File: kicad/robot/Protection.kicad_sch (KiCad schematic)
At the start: 44 parts, among them IC1 TPS22998RYZR, Q1 Q_NMOS_GDS, Q2 EFC8811R-TF, SW1 SW_SPST, U12 BQ27742YZFR-G1

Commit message: BOM exclusions for net ties and n/a part test points
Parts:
- TP28, TP29: now left out of the parts list
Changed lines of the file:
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@@
   )
   (symbol (lib_id "robot:TestPoint") (at 394.97 80.01 0) (unit 1)
-    (in_bom yes) (on_board yes) (dnp no) (fields_autoplaced)
+    (in_bom no) (on_board yes) (dnp no) (fields_autoplaced)
     (property "Reference" "TP29" (at 397.51 76.708 0)
       (effects (font (size 1.27 1.27)) (justify left))
@@
   )
   (symbol (lib_id "robot:TestPoint") (at 43.18 133.35 90) (unit 1)
-    (in_bom yes) (on_board yes) (dnp no) (fields_autoplaced)
+    (in_bom no) (on_board yes) (dnp no) (fields_autoplaced)
     (property "Reference" "TP28" (at 39.878 130.81 90)
       (effects (font (size 1.27 1.27)))

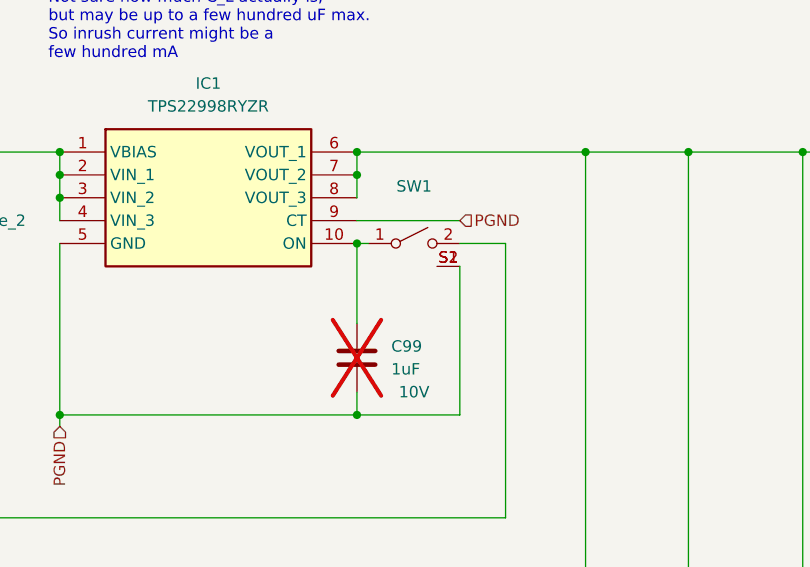
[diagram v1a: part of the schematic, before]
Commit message: Switch wasn't added for some reason
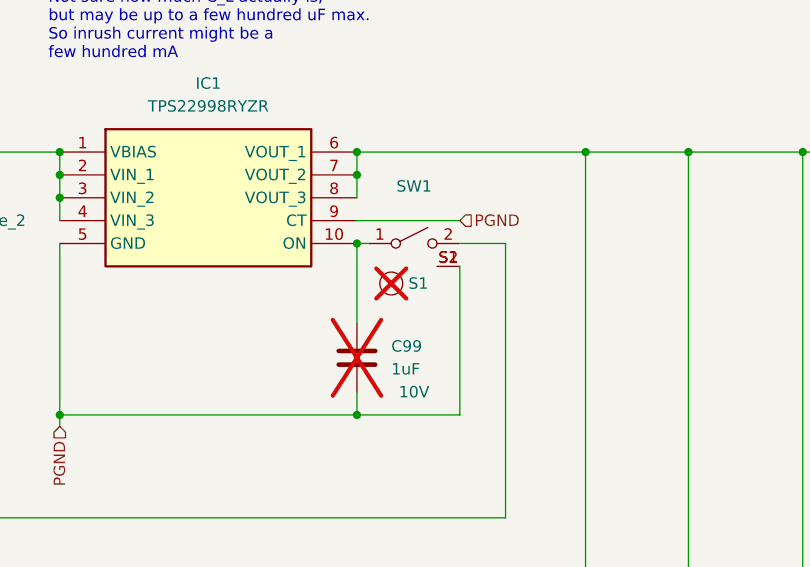
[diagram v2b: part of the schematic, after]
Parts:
- added S1: ~, symbol robot:SW-R3-1A-A-1-2
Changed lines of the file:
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@@
+    )
+  )
+  (symbol (lib_id "robot:SW-R3-1A-A-1-2") (at 319.405 95.885 0) (unit 1)
+    (in_bom yes) (on_board no) (dnp yes) (fields_autoplaced)
+    (property "Reference" "S1" (at 321.31 95.885 0)
+      (effects (font (size 1.27 1.27)) (justify left))
+    )
+    (property "Value" "~" (at 319.405 95.885 0)
+      (effects (font (size 1.27 1.27)) hide)
+    )
+    (property "Footprint" "" (at 319.405 95.885 0)
+      (effects (font (size 1.27 1.27)) hide)
+    )
+    (property "Datasheet" "https://app.adam-tech.com/products/download/data_sheet/203477/sw-r3-1a-a-xx-2-data-sheet.pdf" (at 319.405 95.885 0)
+      (effects (font (size 1.27 1.27)) hide)
+    )
+    (property "Manufacturer" "Adam Tech" (at 319.405 95.885 0)
+      (effects (font (size 1.27 1.27)) hide)
+    )
+    (property "Part Number" "SW-R3-1A-A-1-2" (at 319.405 95.885 0)
+      (effects (font (size 1.27 1.27)) hide)
+    )
+    (instances
+      (project "robot"
+        (path "/0c7b298e-2d07-4b1f-b033-e95f02d45089/aaf20b87-68dc-43c9-a7d3-4ceda8b87424"
+          (reference "S1") (unit 1)
+        )
+      )
     )
   )

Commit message: Updating part number for 0805 100uF caps
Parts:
- C106, C107, C108, C96, C98: Part Number GRM31CD80J107MEA8K -> GRM21BR60E107ME15K
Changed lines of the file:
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@@
       (effects (font (size 1.27 1.27)) hide)
     )
-    (property "Part Number" "GRM31CD80J107MEA8K" (at 365.125 138.43 0)
+    (property "Part Number" "GRM21BR60E107ME15K" (at 365.125 138.43 0)
       (effects (font (size 1.27 1.27)) hide)
     )
@@
       (effects (font (size 1.27 1.27)) hide)
     )
-    (property "Part Number" "GRM31CD80J107MEA8K" (at 264.16 138.43 0)
+    (property "Part Number" "GRM21BR60E107ME15K" (at 264.16 138.43 0)
       (effects (font (size 1.27 1.27)) hide)
     )
@@
       (effects (font (size 1.27 1.27)) hide)
     )
-    (property "Part Number" "GRM31CD80J107MEA8K" (at 352.425 138.43 0)
+    (property "Part Number" "GRM21BR60E107ME15K" (at 352.425 138.43 0)
       (effects (font (size 1.27 1.27)) hide)
     )
@@
       (effects (font (size 1.27 1.27)) hide)
     )
-    (property "Part Number" "GRM31CD80J107MEA8K" (at 378.46 138.43 0)
+    (property "Part Number" "GRM21BR60E107ME15K" (at 378.46 138.43 0)
       (effects (font (size 1.27 1.27)) hide)
     )
@@
       (effects (font (size 1.27 1.27)) hide)
     )
-    (property "Part Number" "GRM31CD80J107MEA8K" (at 340.995 138.43 0)
-      (effects (font (size 1.27 1.27)) hide)
-    )
+    (property "Part Number" "GRM21BR60E107ME15K" (at 340.995 138.43 0)
+      (effects (font (size 1.27 1.27)) hide)
+    )

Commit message: All BOM and footprints other than 100uF selected
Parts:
- C106, C107, C108, C96, C98: Part Number GRM21BR60E107ME15K -> (none)
- R43, R45: Manufacturer Panasonic Electronic Components -> Panasonic; Part Number ERJ-PA3F2000V -> ERJ-PA3J201V
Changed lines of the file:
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@@
       (effects (font (size 1.27 1.27)) hide)
     )
-    (property "Part Number" "GRM21BR60E107ME15K" (at 365.125 138.43 0)
+    (property "Part Number" "" (at 365.125 138.43 0)
       (effects (font (size 1.27 1.27)) hide)
     )
@@
       (effects (font (size 1.27 1.27)) hide)
     )
-    (property "Part Number" "GRM21BR60E107ME15K" (at 264.16 138.43 0)
+    (property "Part Number" "" (at 264.16 138.43 0)
       (effects (font (size 1.27 1.27)) hide)
     )
@@
       (effects (font (size 1.27 1.27)) hide)
     )
-    (property "Part Number" "GRM21BR60E107ME15K" (at 352.425 138.43 0)
+    (property "Part Number" "" (at 352.425 138.43 0)
       (effects (font (size 1.27 1.27)) hide)
     )
@@
       (effects (font (size 1.27 1.27)) hide)
     )
-    (property "Manufacturer" "Panasonic Electronic Components" (at 150.495 98.425 0)
-      (effects (font (size 1.27 1.27)) hide)
-    )
-    (property "Part Number" "ERJ-PA3F2000V" (at 150.495 98.425 0)
+    (property "Manufacturer" "Panasonic" (at 150.495 98.425 0)
+      (effects (font (size 1.27 1.27)) hide)
+    )
+    (property "Part Number" "ERJ-PA3J201V" (at 150.495 98.425 0)
       (effects (font (size 1.27 1.27)) hide)
     )
@@
       (effects (font (size 1.27 1.27)) hide)
     )
-    (property "Part Number" "GRM21BR60E107ME15K" (at 378.46 138.43 0)
+    (property "Part Number" "" (at 378.46 138.43 0)
       (effects (font (size 1.27 1.27)) hide)
     )
@@
       (effects (font (size 1.27 1.27)) hide)
     )
-    (property "Part Number" "GRM21BR60E107ME15K" (at 340.995 138.43 0)
+    (property "Part Number" "" (at 340.995 138.43 0)
       (effects (font (size 1.27 1.27)) hide)
     )
@@
       (effects (font (size 1.27 1.27)) hide)
     )
-    (property "Manufacturer" "Panasonic Electronic Components" (at 170.815 98.425 0)
-      (effects (font (size 1.27 1.27)) hide)
-    )
-    (property "Part Number" "ERJ-PA3F2000V" (at 170.815 98.425 0)
-      (effects (font (size 1.27 1.27)) hide)
-    )
+    (property "Manufacturer" "Panasonic" (at 170.815 98.425 0)
+      (effects (font (size 1.27 1.27)) hide)
+    )
+    (property "Part Number" "ERJ-PA3J201V" (at 170.815 98.425 0)
+      (effects (font (size 1.27 1.27)) hide)
+    )

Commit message: Updated 100uF caps to 1206 footprint to allow for 6.3V ratings
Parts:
- C106, C107, C108, C96, C98: footprint robot:C_0805_2012Metric -> robot:C_1206_3216Metric; Part Number (none) -> GRM31CD80J107MEA8K
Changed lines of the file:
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@@
       (effects (font (size 1.27 1.27)) (justify left))
     )
-    (property "Footprint" "robot:C_0805_2012Metric" (at 366.0902 142.24 0)
+    (property "Footprint" "robot:C_1206_3216Metric" (at 366.0902 142.24 0)
       (effects (font (size 1.27 1.27)) hide)
     )
@@
       (effects (font (size 1.27 1.27)) hide)
     )
-    (property "Part Number" "" (at 365.125 138.43 0)
+    (property "Part Number" "GRM31CD80J107MEA8K" (at 365.125 138.43 0)
       (effects (font (size 1.27 1.27)) hide)
     )
@@
       (effects (font (size 1.27 1.27)) (justify left))
     )
-    (property "Footprint" "robot:C_0805_2012Metric" (at 265.1252 142.24 0)
+    (property "Footprint" "robot:C_1206_3216Metric" (at 265.1252 142.24 0)
       (effects (font (size 1.27 1.27)) hide)
     )
@@
       (effects (font (size 1.27 1.27)) hide)
     )
-    (property "Part Number" "" (at 264.16 138.43 0)
+    (property "Part Number" "GRM31CD80J107MEA8K" (at 264.16 138.43 0)
       (effects (font (size 1.27 1.27)) hide)
     )
@@
       (effects (font (size 1.27 1.27)) (justify left))
     )
-    (property "Footprint" "robot:C_0805_2012Metric" (at 353.3902 142.24 0)
+    (property "Footprint" "robot:C_1206_3216Metric" (at 353.3902 142.24 0)
       (effects (font (size 1.27 1.27)) hide)
     )
@@
       (effects (font (size 1.27 1.27)) hide)
     )
-    (property "Part Number" "" (at 352.425 138.43 0)
+    (property "Part Number" "GRM31CD80J107MEA8K" (at 352.425 138.43 0)
       (effects (font (size 1.27 1.27)) hide)
     )
@@
       (effects (font (size 1.27 1.27)) (justify left))
     )
-    (property "Footprint" "robot:C_0805_2012Metric" (at 379.4252 142.24 0)
+    (property "Footprint" "robot:C_1206_3216Metric" (at 379.4252 142.24 0)
       (effects (font (size 1.27 1.27)) hide)
     )
@@
       (effects (font (size 1.27 1.27)) hide)
     )
-    (property "Part Number" "" (at 378.46 138.43 0)
+    (property "Part Number" "GRM31CD80J107MEA8K" (at 378.46 138.43 0)
       (effects (font (size 1.27 1.27)) hide)
     )
@@
       (effects (font (size 1.27 1.27)) (justify left))
     )
-    (property "Footprint" "robot:C_0805_2012Metric" (at 341.9602 142.24 0)
+    (property "Footprint" "robot:C_1206_3216Metric" (at 341.9602 142.24 0)
       (effects (font (size 1.27 1.27)) hide)
     )
@@
       (effects (font (size 1.27 1.27)) hide)
     )
-    (property "Part Number" "" (at 340.995 138.43 0)
-      (effects (font (size 1.27 1.27)) hide)
-    )
+    (property "Part Number" "GRM31CD80J107MEA8K" (at 340.995 138.43 0)
+      (effects (font (size 1.27 1.27)) hide)
+    )

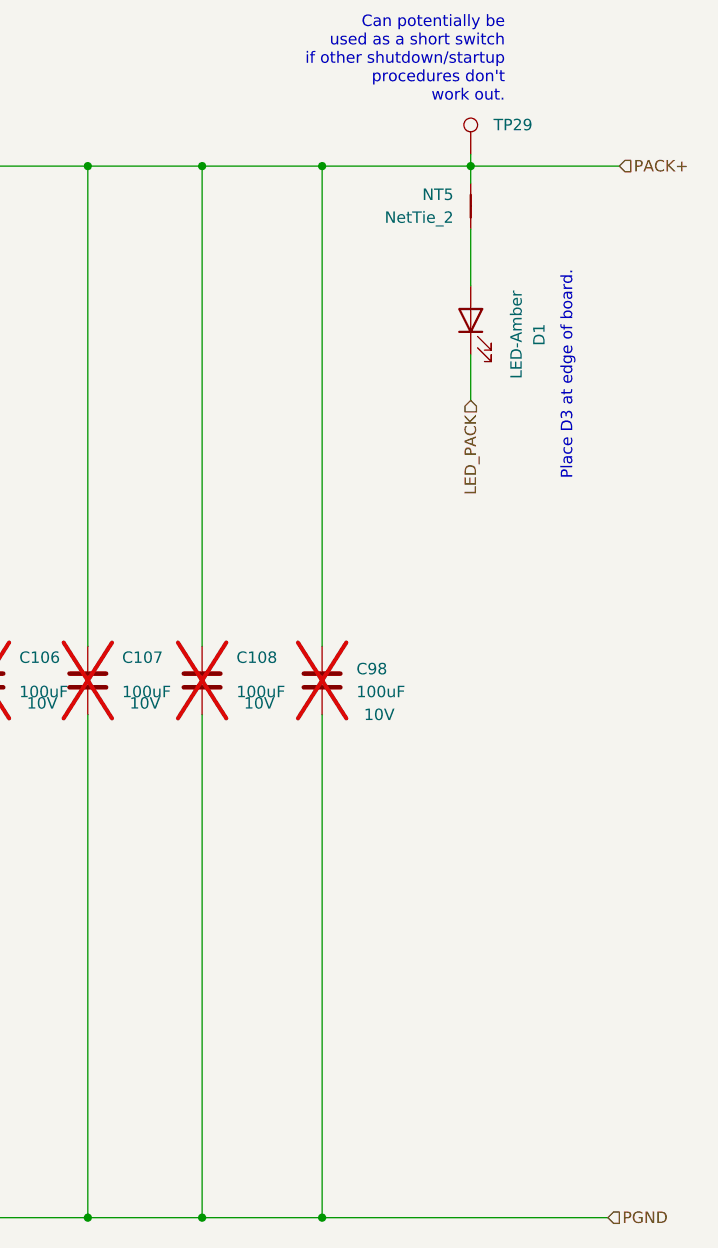
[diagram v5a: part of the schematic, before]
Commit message: Adding wireless charger circuit
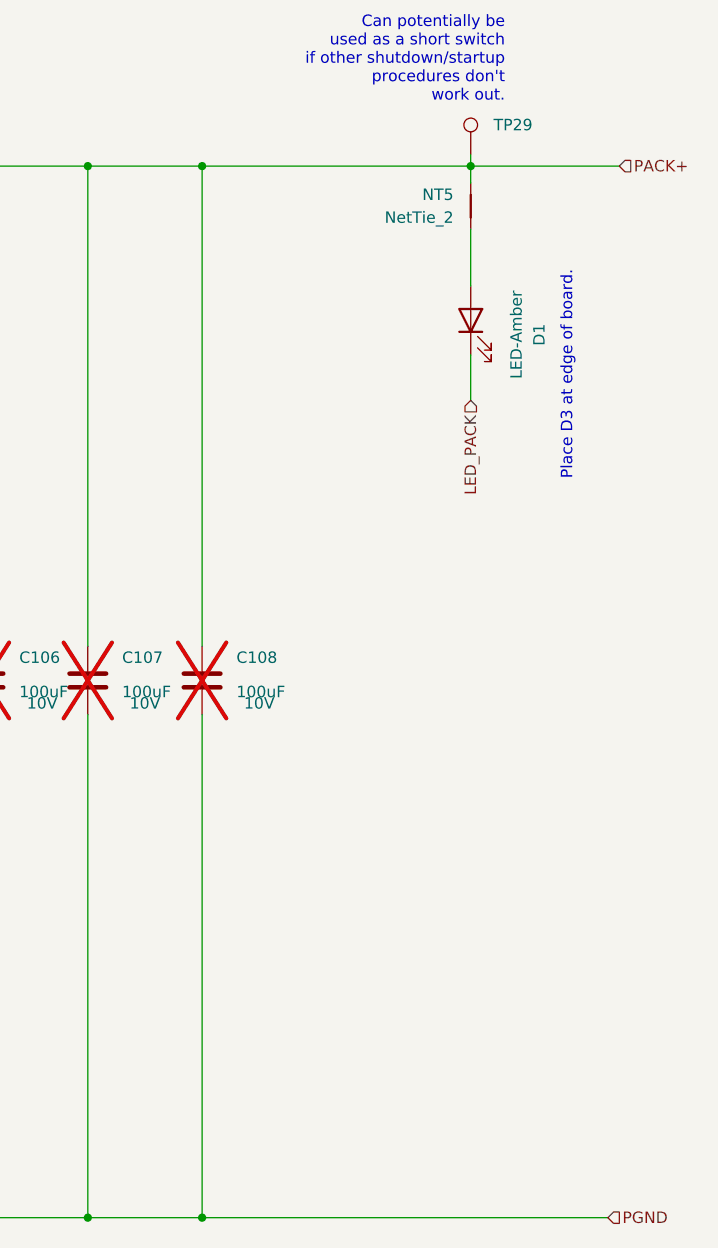
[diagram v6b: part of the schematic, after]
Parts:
- removed C98: 100uF, robot:C_1206_3216Metric, symbol robot:C
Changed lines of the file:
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@@
   (junction (at 282.575 81.28) (diameter 0) (color 0 0 0 0)
   )
-  (junction (at 378.46 81.28) (diameter 0) (color 0 0 0 0)
-  )
   (junction (at 227.965 135.89) (diameter 0) (color 0 0 0 0)
   )
@@
   )
   (junction (at 352.425 81.28) (diameter 0) (color 0 0 0 0)
-  )
-  (junction (at 378.46 198.12) (diameter 0) (color 0 0 0 0)
   )
   (junction (at 170.815 81.28) (diameter 0) (color 0 0 0 0)
@@
     (stroke (width 0) (type default))
   )
-  (wire (pts (xy 378.46 198.12) (xy 410.21 198.12))
+  (wire (pts (xy 365.125 198.12) (xy 410.21 198.12))
     (stroke (width 0) (type default))
   )
@@
     (stroke (width 0) (type default))
   )
-  (wire (pts (xy 378.46 142.24) (xy 378.46 198.12))
-    (stroke (width 0) (type default))
-  )
   (wire (pts (xy 43.18 81.28) (xy 150.495 81.28))
     (stroke (width 0) (type default))
@@
     (stroke (width 0) (type default))
   )
-  (wire (pts (xy 378.46 81.28) (xy 394.97 81.28))
+  (wire (pts (xy 365.125 81.28) (xy 394.97 81.28))
     (stroke (width 0) (type default))
   )
@@
     (stroke (width 0) (type default))
   )
-  (wire (pts (xy 365.125 81.28) (xy 378.46 81.28))
-    (stroke (width 0) (type default))
-  )
   (wire (pts (xy 203.2 101.6) (xy 203.2 109.22))
     (stroke (width 0) (type default))
@@
     (stroke (width 0) (type default))
   )
-  (wire (pts (xy 378.46 81.28) (xy 378.46 134.62))
-    (stroke (width 0) (type default))
-  )
   (wire (pts (xy 140.97 156.21) (xy 158.75 156.21))
     (stroke (width 0) (type default))
@@
   )
   (wire (pts (xy 315.595 91.44) (xy 316.865 91.44))
-    (stroke (width 0) (type default))
-  )
-  (wire (pts (xy 365.125 198.12) (xy 378.46 198.12))
     (stroke (width 0) (type default))
   )
@@
         )
       )
-    )
-  )
-  (symbol (lib_id "robot:C") (at 378.46 138.43 0) (unit 1)
-    (in_bom yes) (on_board yes) (dnp yes)
-    (property "Reference" "C98" (at 382.27 137.1599 0)
-      (effects (font (size 1.27 1.27)) (justify left))
-    )
-    (property "Value" "100uF" (at 382.27 139.6999 0)
-      (effects (font (size 1.27 1.27)) (justify left))
-    )
-    (property "Footprint" "robot:C_1206_3216Metric" (at 379.4252 142.24 0)
-      (effects (font (size 1.27 1.27)) hide)
-    )
-    (property "Datasheet" "~" (at 378.46 138.43 0)
-      (effects (font (size 1.27 1.27)) hide)
-    )
-    (property "Description" "10V" (at 384.81 142.24 0)
-      (effects (font (size 1.27 1.27)))
-    )
-    (property "Manufacturer" "Murata" (at 378.46 138.43 0)
-      (effects (font (size 1.27 1.27)) hide)
-    )
-    (property "Part Number" "GRM31CD80J107MEA8K" (at 378.46 138.43 0)
-      (effects (font (size 1.27 1.27)) hide)
-    )
-    (property "Stock" "" (at 378.46 138.43 0)
-      (effects (font (size 1.27 1.27)) hide)
-    )
-    (pin "1")
-    (pin "2")
-    (instances
-      (project "robot"
-        (path "/0c7b298e-2d07-4b1f-b033-e95f02d45089/aaf20b87-68dc-43c9-a7d3-4ceda8b87424"
-          (reference "C98") (unit 1)
-        )
-      )

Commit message: Updating stock on digikey parts delivered
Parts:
- C106, C107, C108, C96: Stock (none) -> 20; V_Max (none) -> 6.3V
- C55, C99: Stock (none) -> 10
- S1: Stock (none) -> 5
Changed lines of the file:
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@@
       (effects (font (size 1.27 1.27)) hide)
     )
-    (property "Stock" "" (at 315.595 104.14 0)
+    (property "Stock" "10" (at 315.595 104.14 0)
       (effects (font (size 1.27 1.27)) hide)
     )
@@
       (effects (font (size 1.27 1.27)) hide)
     )
-    (property "Stock" "" (at 365.125 138.43 0)
+    (property "Stock" "20" (at 365.125 138.43 0)
+      (effects (font (size 1.27 1.27)) hide)
+    )
+    (property "V_Max" "6.3V" (at 365.125 138.43 0)
       (effects (font (size 1.27 1.27)) hide)
     )
@@
       (effects (font (size 1.27 1.27)) hide)
     )
-    (property "Stock" "" (at 71.12 142.24 0)
+    (property "Stock" "10" (at 71.12 142.24 0)
       (effects (font (size 1.27 1.27)) hide)
     )
@@
       (effects (font (size 1.27 1.27)) hide)
     )
+    (property "Stock" "5" (at 319.405 95.885 0)
+      (effects (font (size 1.27 1.27)) hide)
+    )
     (instances
       (project "robot"
@@
       (effects (font (size 1.27 1.27)) hide)
     )
-    (property "Stock" "" (at 264.16 138.43 0)
+    (property "Stock" "20" (at 264.16 138.43 0)
+      (effects (font (size 1.27 1.27)) hide)
+    )
+    (property "V_Max" "6.3V" (at 264.16 138.43 0)
       (effects (font (size 1.27 1.27)) hide)
     )
@@
       (effects (font (size 1.27 1.27)) hide)
     )
-    (property "Stock" "" (at 352.425 138.43 0)
+    (property "Stock" "20" (at 352.425 138.43 0)
+      (effects (font (size 1.27 1.27)) hide)
+    )
+    (property "V_Max" "6.3V" (at 352.425 138.43 0)
       (effects (font (size 1.27 1.27)) hide)
     )
@@
       (effects (font (size 1.27 1.27)) hide)
     )
-    (property "Stock" "" (at 340.995 138.43 0)
-      (effects (font (size 1.27 1.27)) hide)
-    )
+    (property "Stock" "20" (at 340.995 138.43 0)
+      (effects (font (size 1.27 1.27)) hide)
+    )
+    (property "V_Max" "6.3V" (at 340.995 138.43 0)
+      (effects (font (size 1.27 1.27)) hide)
+    )

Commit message: Adding 5 to stock of BatteryHolder_26650
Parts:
- BT1: Stock (none) -> 5
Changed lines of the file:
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@@
       (effects (font (size 1.27 1.27)) hide)
     )
-    (property "Stock" "" (at 46.99 152.4 0)
+    (property "Stock" "5" (at 46.99 152.4 0)
       (effects (font (size 1.27 1.27)) hide)
     )
